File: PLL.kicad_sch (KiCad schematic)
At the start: 0 parts

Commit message: Phase detector completed
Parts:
- added R1, R2: 10k, Resistor_THT:R_Axial_DIN0207_L6.3mm_D2.5mm_P7.62mm_Horizontal, symbol Device:R
- added U1: 74HC74, Package_DIP:DIP-14_W7.62mm, symbol 74xx:74HC74
- added U2: 7400, Package_DIP:DIP-14_W7.62mm, symbol 74xx:7400
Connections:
- new net: R1.2, U1.2 (D)
- new net: R2.2, U1.12 (D)
- new net DOWN: U1.9 (Q), U2.1
- new net GND_D: U1.7 (GND), U2.7 (GND)
- new net UP: U1.5 (Q), U2.2
- new net VCC: R1.1, R2.1, U1.10 (~{S}), U1.14 (VCC), U1.4 (~{S}), U2.14 (VCC)
- new net ~{R}: U1.1 (~{R}), U1.13 (~{R}), U2.3
- no-connect marks 0 -> 2

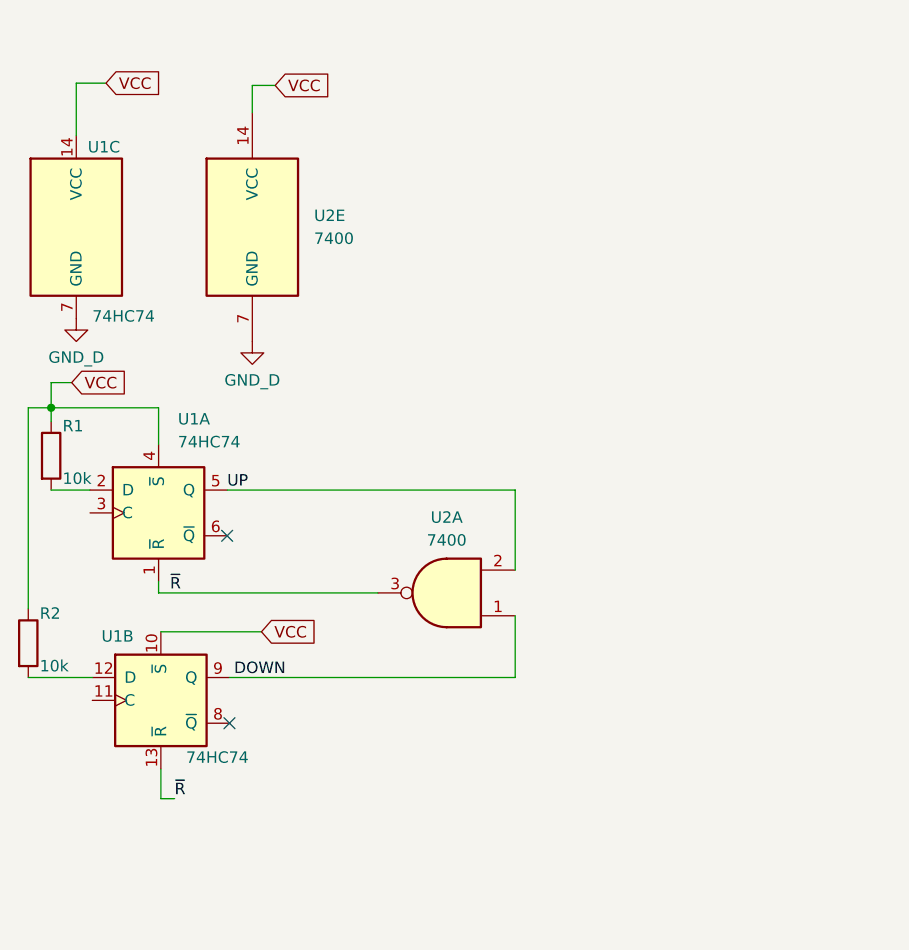
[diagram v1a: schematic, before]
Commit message: BJT push-pull charge pump added
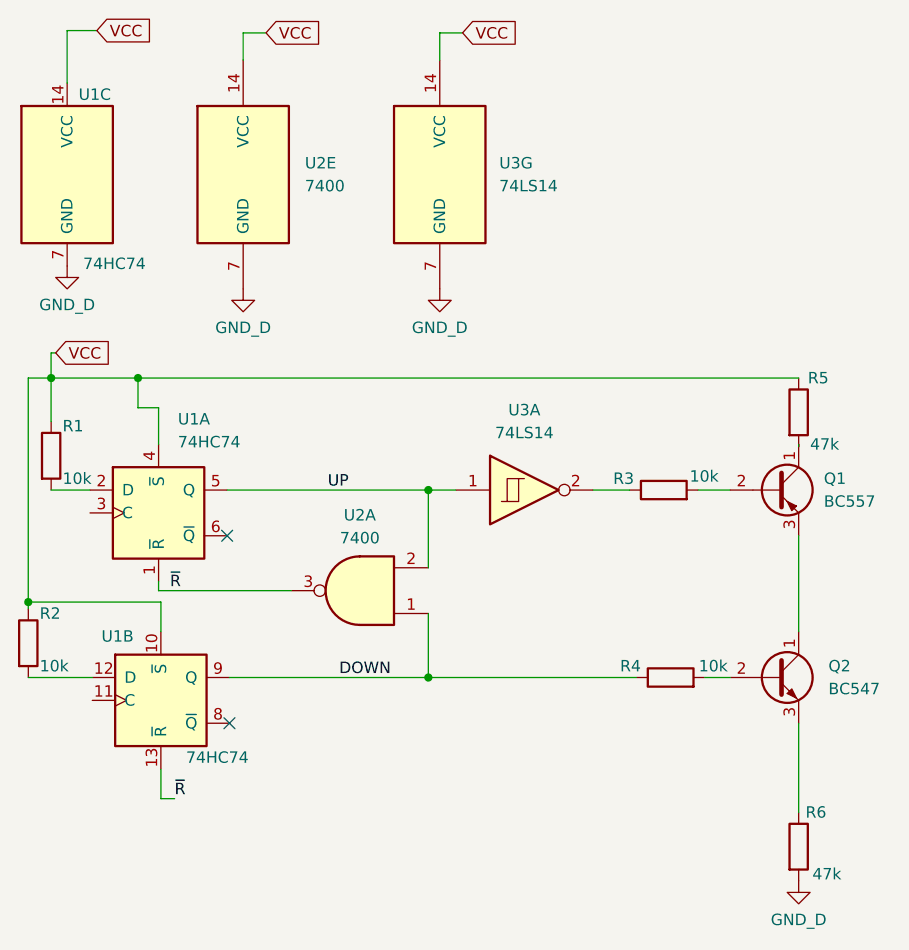
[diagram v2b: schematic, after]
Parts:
- added Q1: BC557, Package_TO_SOT_THT:TO-92_Inline, symbol Transistor_BJT:BC557
- added Q2: BC547, Package_TO_SOT_THT:TO-92_Inline, symbol Transistor_BJT:BC547
- added R3, R4: 10k, Resistor_THT:R_Axial_DIN0207_L6.3mm_D2.5mm_P7.62mm_Horizontal, symbol Device:R
- added R5, R6: 47k, symbol Device:R
- added U3: 74LS14, symbol 74xx:74LS14
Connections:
- net DOWN: now also R4.1
- net GND_D: now also R6.2, U3.7 (GND)
- net UP: now also U3.1
- net VCC: now also R5.1, U3.14 (VCC)
- new net: R3.1, U3.2
- new net: Q1.2 (B), R3.2
- new net: Q2.3 (E), R6.1
- new net: Q1.3 (E), Q2.1 (C)
- new net: Q2.2 (B), R4.2
- new net: Q1.1 (C), R5.2
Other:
- moved on the sheet: U1C, U2A, U2E

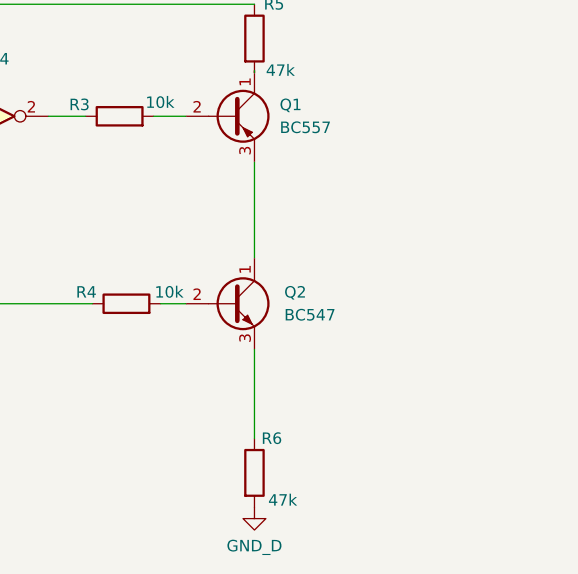
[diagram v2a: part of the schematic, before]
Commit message: Added Low-Pass Filter and footprints for resistors
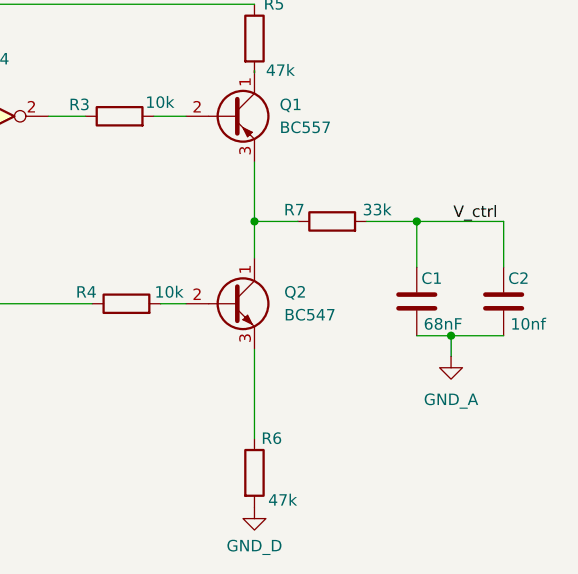
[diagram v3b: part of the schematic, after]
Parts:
- added C1: 68nF, Capacitor_THT:C_Disc_D3.0mm_W1.6mm_P2.50mm, symbol Device:C
- added C2: 10nf, Capacitor_THT:C_Disc_D3.0mm_W1.6mm_P2.50mm, symbol Device:C
- added R7: 33k, Resistor_THT:R_Axial_DIN0207_L6.3mm_D2.5mm_P7.62mm_Horizontal, symbol Device:R
- R5, R6: footprint (none) -> Resistor_THT:R_Axial_DIN0207_L6.3mm_D2.5mm_P7.62mm_Horizontal
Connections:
- net at Q1.3 (E), Q2.1 (C): now also R7.1
- new net GND_A: C1.2, C2.2
- new net V_ctrl: C1.1, C2.1, R7.2

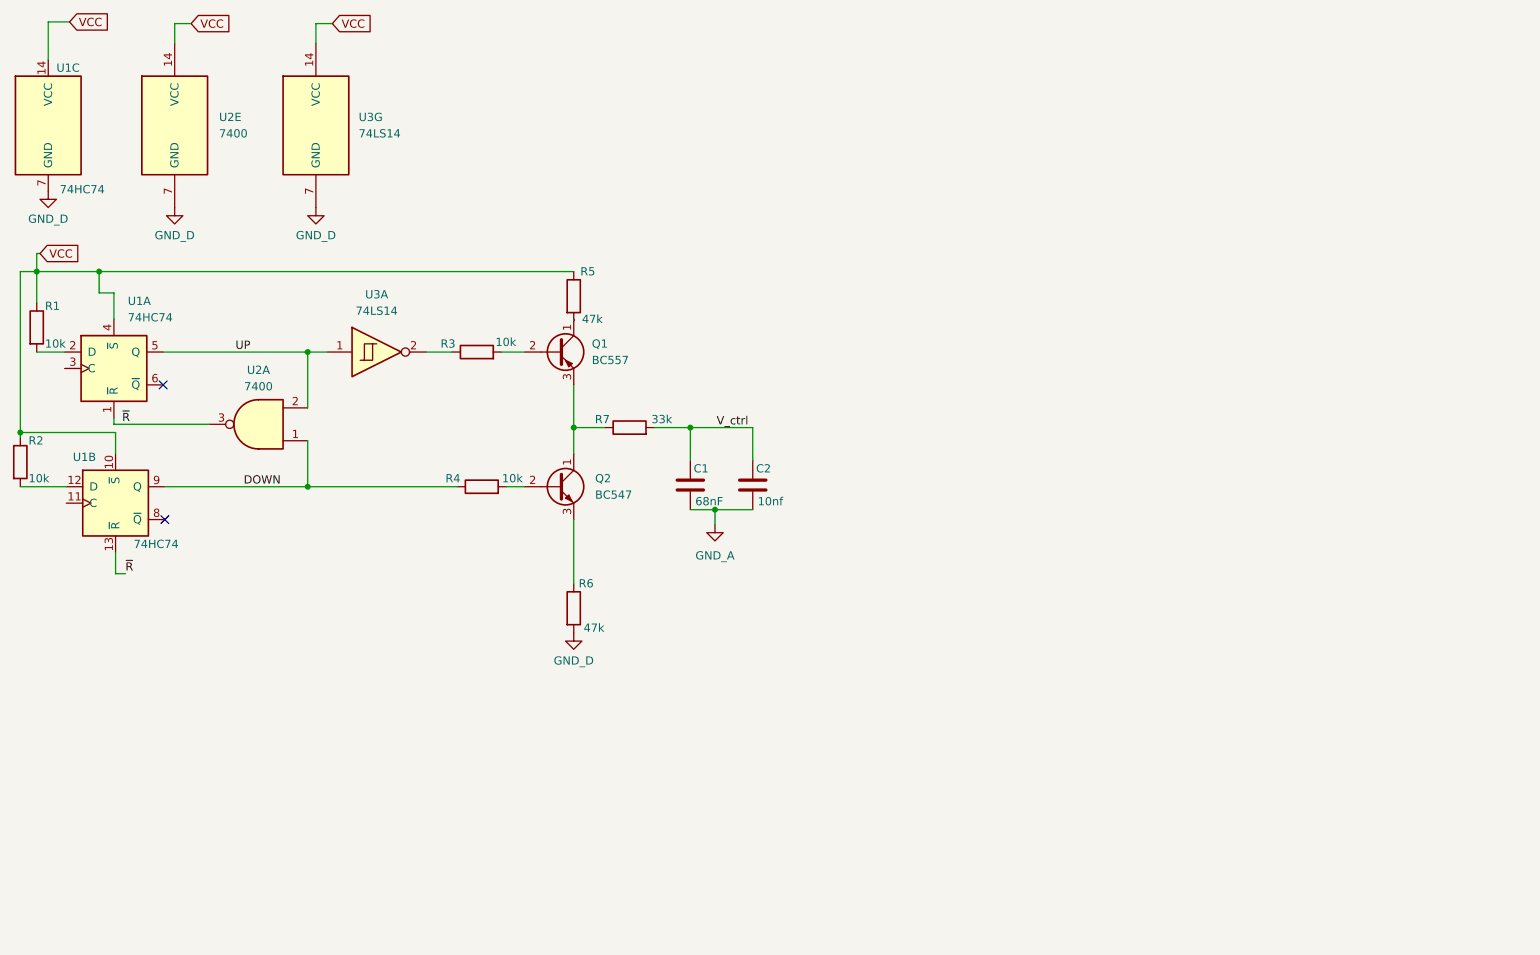
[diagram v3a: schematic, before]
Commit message: 555 Timer Voltage controlled oscillator circuitry added
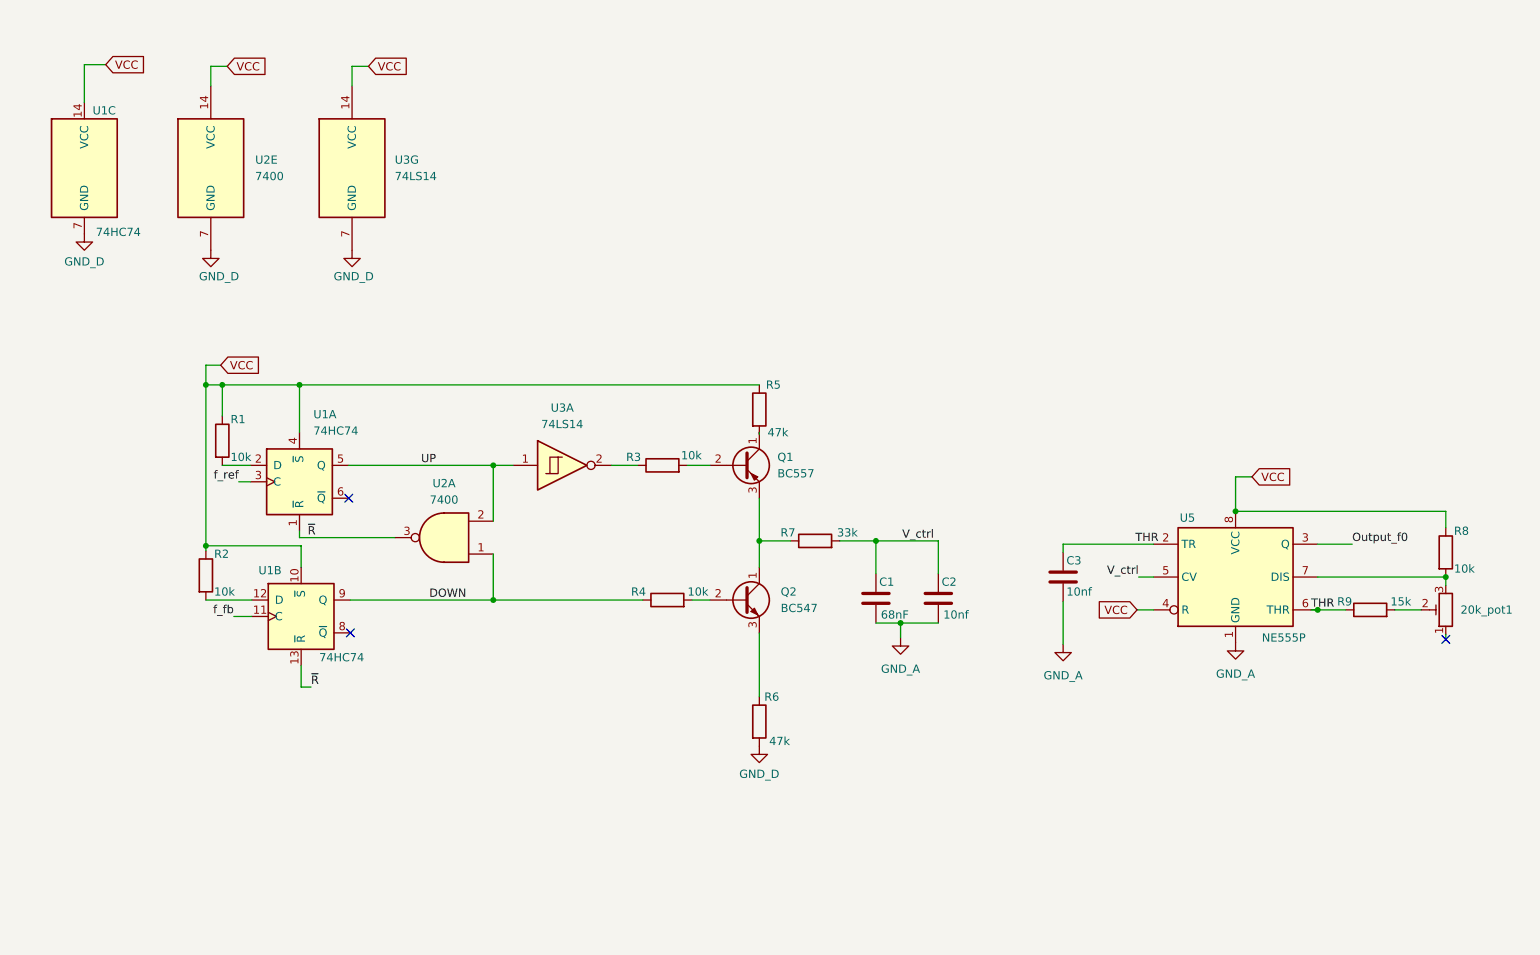
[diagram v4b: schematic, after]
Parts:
- added 20k_pot1: R_Potentiometer_Trim, Potentiometer_THT:Potentiometer_Runtron_RM-063_Horizontal, symbol Device:R_Potentiometer_Trim
- added C3: 10nf, Capacitor_THT:C_Disc_D3.0mm_W1.6mm_P2.50mm, symbol Device:C
- added R8: 10k, Resistor_THT:R_Axial_DIN0207_L6.3mm_D2.5mm_P7.62mm_Horizontal, symbol Device:R
- added R9: 15k, Resistor_THT:R_Axial_DIN0207_L6.3mm_D2.5mm_P7.62mm_Horizontal, symbol Device:R
- added U5: NE555P, Package_DIP:DIP-8_W7.62mm, symbol Timer:NE555P
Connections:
- net GND_A: now also C3.2, U5.1 (GND)
- net VCC: now also R8.1, U5.4 (R), U5.8 (VCC)
- net V_ctrl: now also U5.5 (CV)
- net f_fb: now reaches U1.11 (C)
- net f_ref: now reaches U1.3 (C)
- new net: 20k_pot1.3, R8.2, U5.7 (DIS)
- new net: 20k_pot1.2, R9.2
- new net Output_f0: U5.3 (Q)
- new net THR: C3.1, R9.1, U5.2 (TR), U5.6 (THR)
- no-connect marks 2 -> 3
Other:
- moved on the sheet: C1, C2, Q1, Q2, R1, R2, R3, R4, R5, R6, R7, U1A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

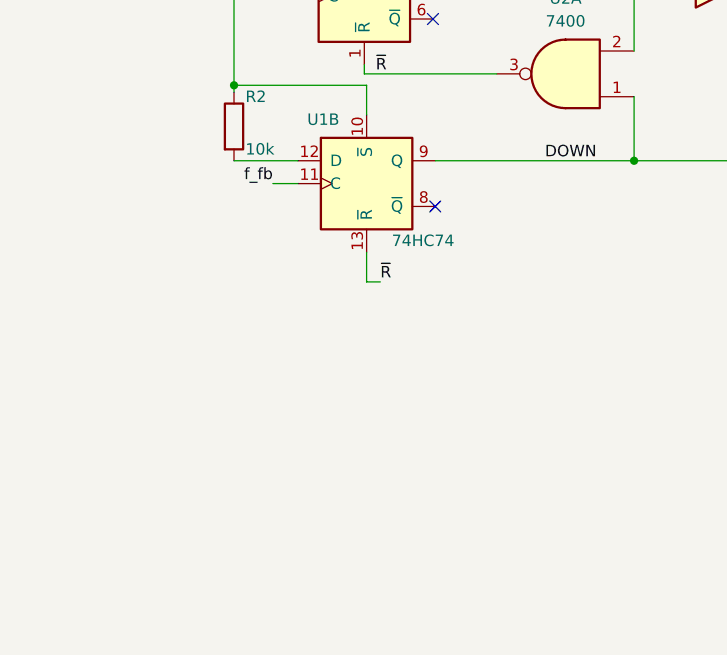
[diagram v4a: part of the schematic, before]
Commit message: Divide by 4 counter added
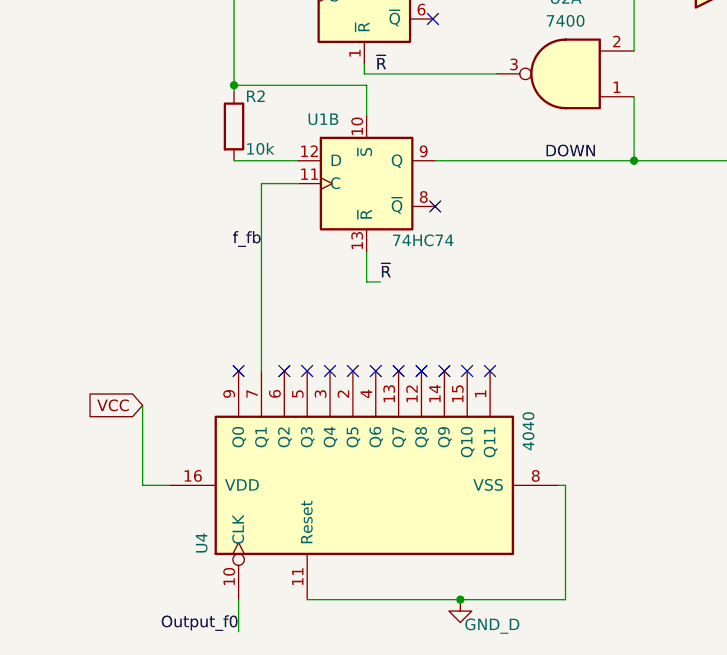
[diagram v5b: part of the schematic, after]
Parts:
- added U4: 4040, Package_DIP:DIP-16_W7.62mm, symbol 4xxx:4040
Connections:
- net GND_D: now also U4.11 (Reset), U4.8 (VSS)
- net Output_f0: now also U4.10 (CLK)
- net VCC: now also U4.16 (VDD)
- net f_fb: now also U4.7 (Q1)
- no-connect marks 3 -> 14
